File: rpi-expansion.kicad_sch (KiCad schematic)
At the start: 15 parts, among them J7 PinHeader_2x20_P2.54mm_Drill1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, J8 JST_SH_1x4_SM04B-SRSS-TB-LF-SN, J9 JST_SH_1x4_SM04B-SRSS-TB-LF-SN, U8 NCP380LSNAJAAT1G

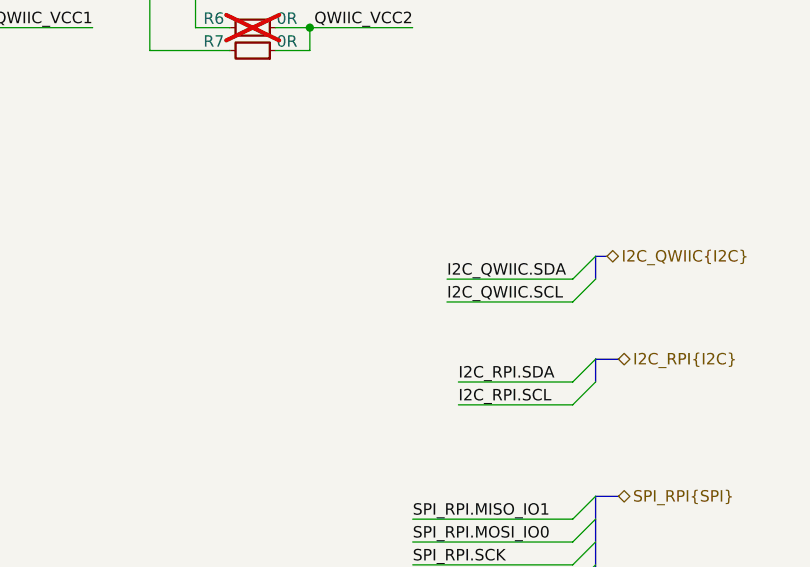
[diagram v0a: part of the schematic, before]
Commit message: [#95036] Add testpoints
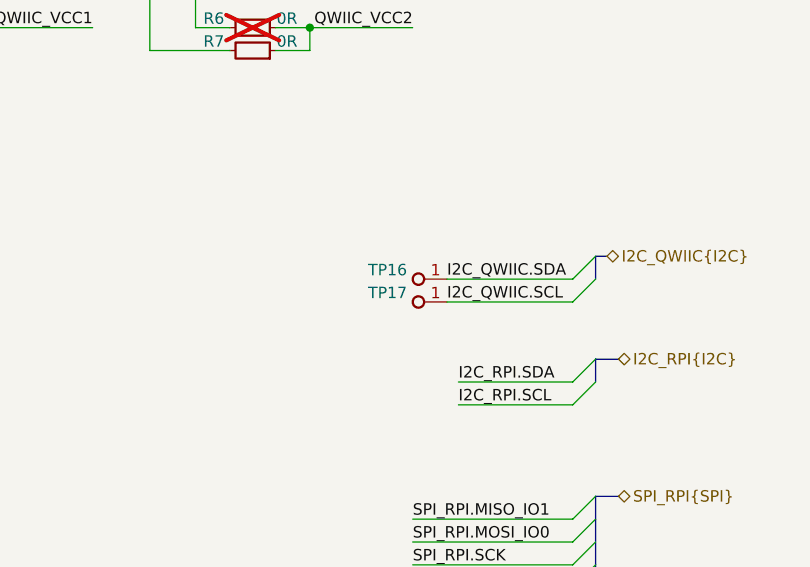
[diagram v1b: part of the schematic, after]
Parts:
- added TP16, TP17: TP_1mm_SMD, antmicro-footprints:TP_SMD_1mm, symbol antmicroTestPoints:TP_1mm_SMD
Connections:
- net I2C_QWIIC.SCL: now also TP17.1
- net I2C_QWIIC.SDA: now also TP16.1
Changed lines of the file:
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@@
+	)
+	(symbol
+		(lib_id "antmicroTestPoints:TP_1mm_SMD")
+		(at 335.28 93.98 180)
+		(unit 1)
+		(exclude_from_sim no)
+		(in_bom no)
+		(on_board yes)
+		(dnp no)
+		(property "Reference" "TP17"
+			(at 328.676 92.964 0)
+			(effects
+				(font
+					(size 1.27 1.27)
+					(thickness 0.15)
+				)
+			)
+		)
+		(property "Value" "TP_1mm_SMD"
+			(at 320.04 86.36 0)
+			(effects
+				(font
+					(size 1.27 1.27)
+					(thickness 0.15)
+				)
+				(justify left bottom)
+				(hide yes)
+			)
+		)
+		(property "Footprint" "antmicro-footprints:TP_SMD_1mm"
+			(at 320.04 83.82 0)
+			(effects
+				(font
+					(size 1.27 1.27)
+					(thickness 0.15)
+				)
+				(justify left bottom)
+				(hide yes)
+			)
+		)
+		(property "Datasheet" ""
+			(at 317.5 81.28 0)
+			(effects
+				(font
+					(size 1.27 1.27)
+					(thickness 0.15)
+				)
+				(justify left bottom)
+				(hide yes)
+			)
+		)
+		(property "Description" "Test point 1mm SMD"
+			(at 320.04 73.66 0)
+			(effects
+				(font
+					(size 1.27 1.27)
+				)
+				(justify left bottom)
+				(hide yes)
+			)
+		)
+		(property "MPN" ""
+			(at 335.28 93.98 0)
+			(effects
+				(font
+					(size 1.27 1.27)
+				)
+				(hide yes)
+			)
+		)
+		(property "Manufacturer" ""
+			(at 335.28 93.98 0)
+			(effects
+				(font
+					(size 1.27 1.27)
+				)
+				(hide yes)
+			)
+		)
+		(property "Author" "Antmicro"
+			(at 320.04 78.74 0)
+			(effects
+				(font
+					(size 1.27 1.27)
+					(thickness 0.15)
+				)
+				(justify left bottom)
+				(hide yes)
+			)
+		)
+		(property "License" "Apache-2.0"
+			(at 320.04 76.2 0)
+			(effects
+				(font
+					(size 1.27 1.27)
+					(thickness 0.15)
+				)
+				(justify left bottom)
+				(hide yes)
+			)
+		)
+		(pin "1"
+		)
+		(instances
+			(project "renode-reference-platform"
+				(path "/126ae87b-f292-4372-94ff-ae46971d67ab/3deaa797-f1d6-4980-9fc1-21264c177bf0"
+					(reference "TP17")
+					(unit 1)
+				)
+			)
+		)
 	)
 	(symbol
@@
 					(unit 1)
 				)
+			)
+		)
+	)
+	(symbol
+		(lib_id "antmicroTestPoints:TP_1mm_SMD")
+		(at 335.28 91.44 180)
+		(unit 1)
+		(exclude_from_sim no)
+		(in_bom no)
+		(on_board yes)
+		(dnp no)
+		(property "Reference" "TP16"
+			(at 328.676 90.424 0)
+			(effects
+				(font
+					(size 1.27 1.27)
+					(thickness 0.15)
+				)
+			)
+		)
+		(property "Value" "TP_1mm_SMD"
+			(at 320.04 83.82 0)
+			(effects
+				(font
+					(size 1.27 1.27)
+					(thickness 0.15)
+				)
+				(justify left bottom)
+				(hide yes)
+			)
+		)
+		(property "Footprint" "antmicro-footprints:TP_SMD_1mm"
+			(at 320.04 81.28 0)
+			(effects
+				(font
+					(size 1.27 1.27)
+					(thickness 0.15)
+				)
+				(justify left bottom)
+				(hide yes)
+			)
+		)
+		(property "Datasheet" ""
+			(at 317.5 78.74 0)
+			(effects
+				(font
+					(size 1.27 1.27)
+					(thickness 0.15)
+				)
+				(justify left bottom)
+				(hide yes)
+			)
+		)
+		(property "Description" "Test point 1mm SMD"
+			(at 320.04 71.12 0)
+			(effects
+				(font
+					(size 1.27 1.27)
+				)
+				(justify left bottom)
+				(hide yes)
+			)
+		)
+		(property "MPN" ""
+			(at 335.28 91.44 0)
+			(effects
+				(font
+					(size 1.27 1.27)
+				)
+				(hide yes)
+			)
+		)
+		(property "Manufacturer" ""
+			(at 335.28 91.44 0)
+			(effects
+				(font
+					(size 1.27 1.27)
+				)
+				(hide yes)
+			)
+		)
+		(property "Author" "Antmicro"
+			(at 320.04 76.2 0)
+			(effects
+				(font
+					(size 1.27 1.27)
+					(thickness 0.15)
+				)
+				(justify left bottom)
+				(hide yes)
+			)
+		)
+		(property "License" "Apache-2.0"
+			(at 320.04 73.66 0)
+			(effects
+				(font
+					(size 1.27 1.27)
+					(thickness 0.15)
+				)
+				(justify left bottom)
+				(hide yes)
+			)
+		)
+		(pin "1"
+		)
+		(instances
+			(project "renode-reference-platform"
+				(path "/126ae87b-f292-4372-94ff-ae46971d67ab/3deaa797-f1d6-4980-9fc1-21264c177bf0"
+					(reference "TP16")
+					(unit 1)
+				)

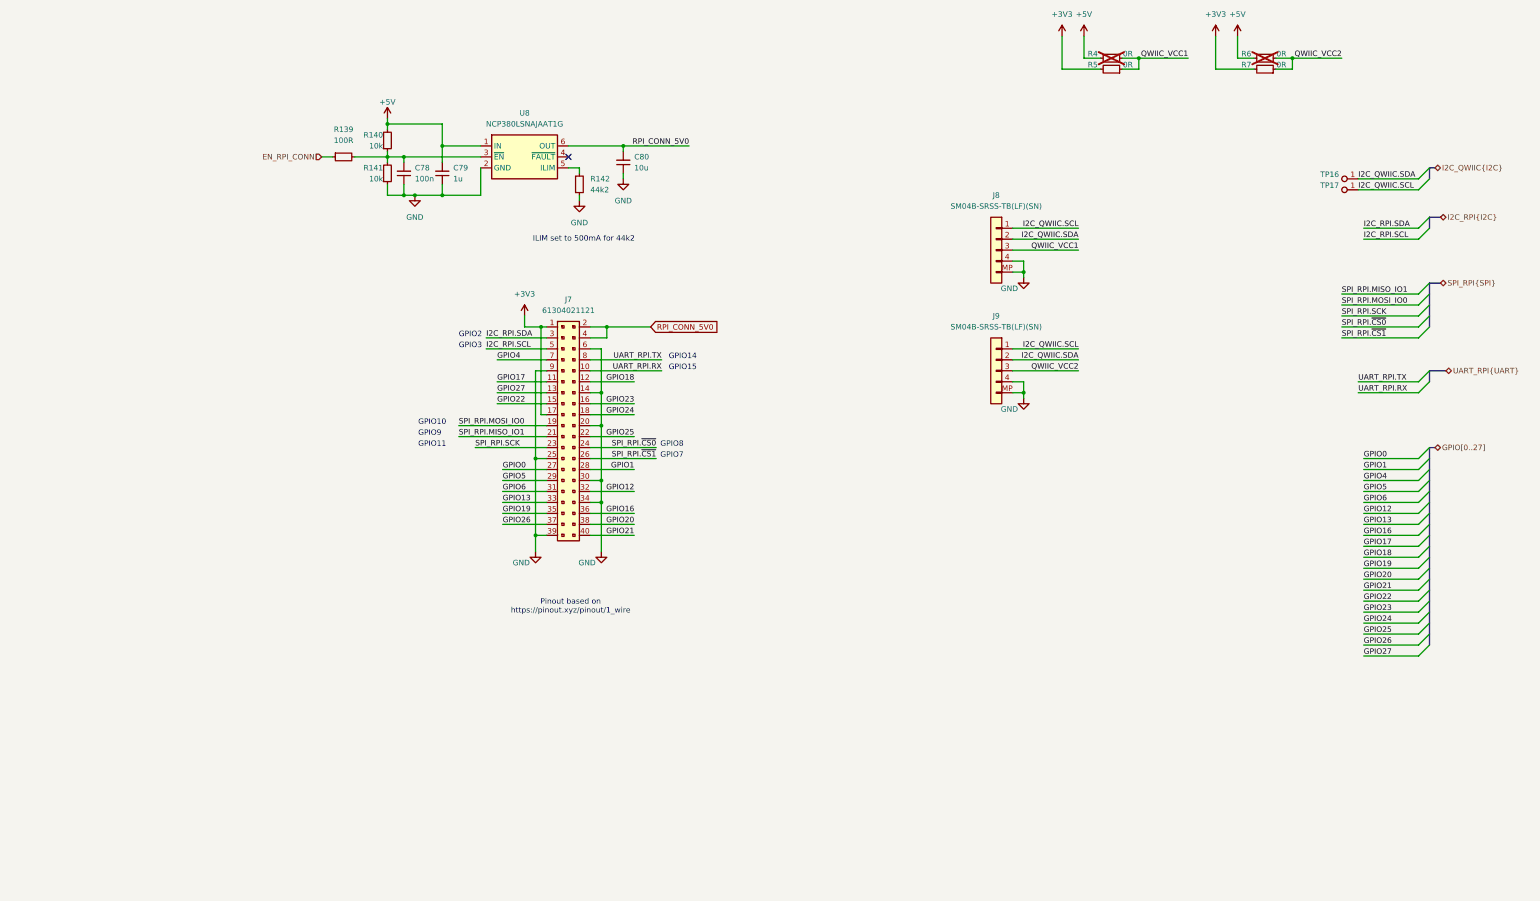
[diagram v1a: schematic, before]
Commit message: [#95036] Add schematic markings
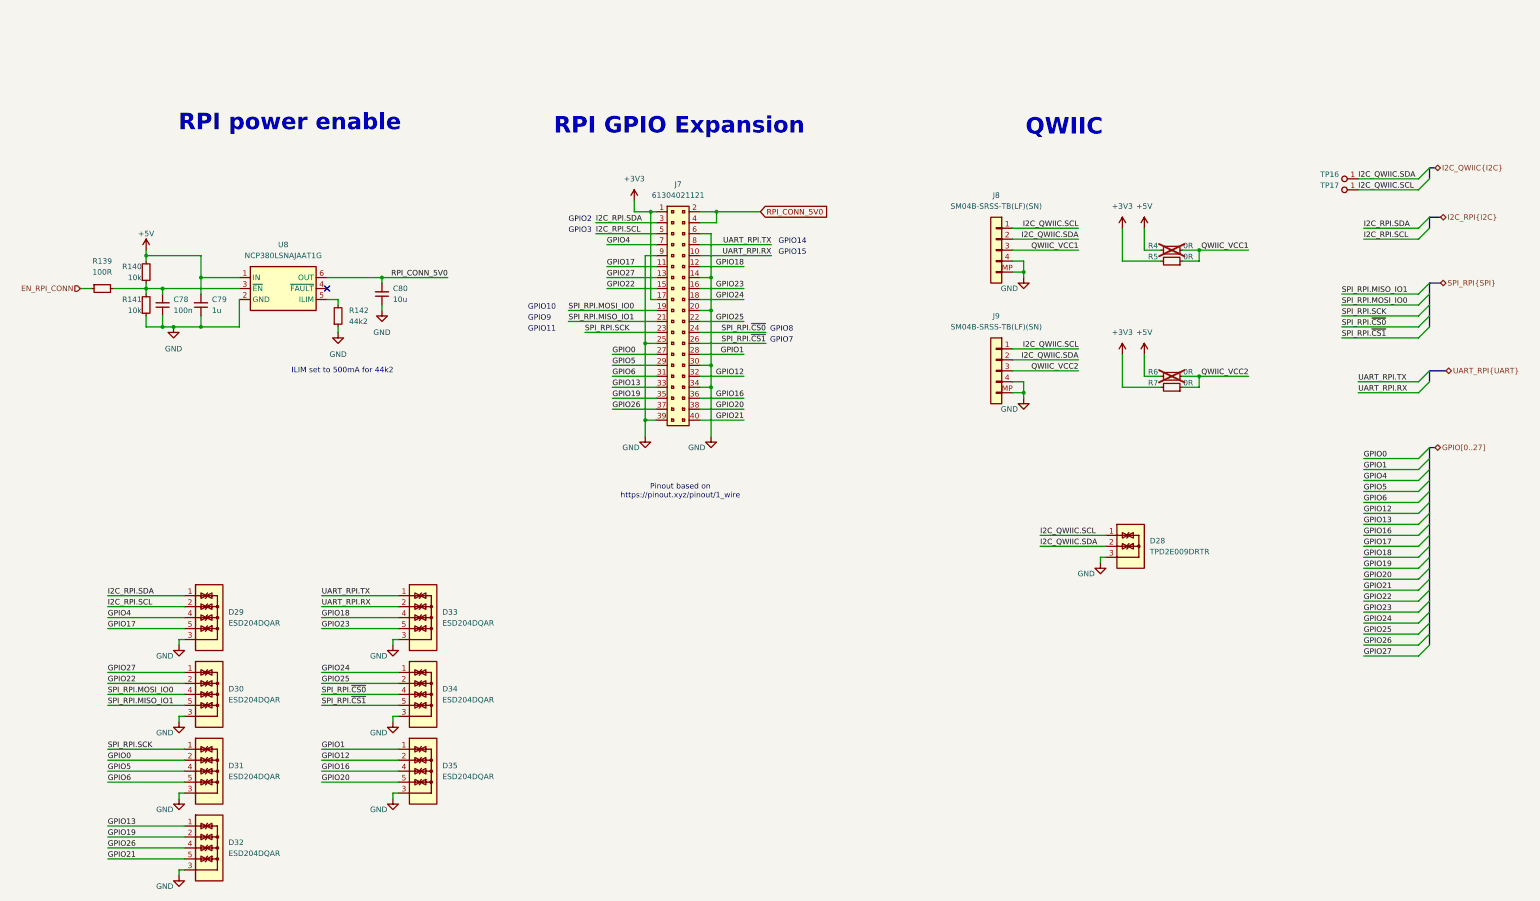
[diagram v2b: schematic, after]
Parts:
- added D28: TPD2E009_SOT-9X3, antmicro-footprints:SOT-723, symbol antmicroTVSDiodes:TPD2E009_SOT-9X3
- added D29, D30, D31, D32, D33, D34, D35: ESD204DQAR, antmicro-footprints:USON-10_2.5x1mm_P0.5mm, symbol antmicroTVSDiodes:ESD204DQAR
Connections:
- net GND: now also D28.3, D29.3, D29.8, D30.3, D30.8, D31.3, D31.8, D32.3, D32.8, D33.3, D33.8, D34.3, D34.8, D35.3, D35.8
- net GPIO0: now also D31.2, D31.9
- net GPIO1: now also D35.1, D35.10
- net GPIO12: now also D35.2, D35.9
- net GPIO13: now also D32.1, D32.10
- net GPIO16: now also D35.4, D35.7
- net GPIO17: now also D29.5, D29.6
- net GPIO18: now also D33.4, D33.7
- net GPIO19: now also D32.2, D32.9
- net GPIO20: now also D35.5, D35.6
- net GPIO21: now also D32.5, D32.6
- net GPIO22: now also D30.2, D30.9
- net GPIO23: now also D33.5, D33.6
- net GPIO24: now also D34.1, D34.10
- net GPIO25: now also D34.2, D34.9
- net GPIO26: now also D32.4, D32.7
- net GPIO27: now also D30.1, D30.10
- net GPIO4: now also D29.4, D29.7
- net GPIO5: now also D31.4, D31.7
- net GPIO6: now also D31.5, D31.6
- net I2C_QWIIC.SCL: now also D28.1
- net I2C_QWIIC.SDA: now also D28.2
- net I2C_RPI.SCL: now also D29.2, D29.9
- net I2C_RPI.SDA: now also D29.1, D29.10
- net SPI_RPI.MISO_IO1: now also D30.5, D30.6
- net SPI_RPI.MOSI_IO0: now also D30.4, D30.7
- net SPI_RPI.SCK: now also D31.1, D31.10
- net SPI_RPI.~{CS0}: now also D34.4, D34.7
- net SPI_RPI.~{CS1}: now also D34.5, D34.6
- net UART_RPI.RX: now also D33.2, D33.9
- net UART_RPI.TX: now also D33.1, D33.10
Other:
- note added: "QWIIC"
- note added: "RPI GPIO Expansion"
- note added: "RPI power enable"
- moved on the sheet: C78, C79, C80, J7, R139, R140, R141, R142, R4, R5, R6, R7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
